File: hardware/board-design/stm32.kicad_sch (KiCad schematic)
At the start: 10 parts, among them J2 Conn_02x05_Odd_Even, SW1 SW_Push, U3 STM32C031C6Ux

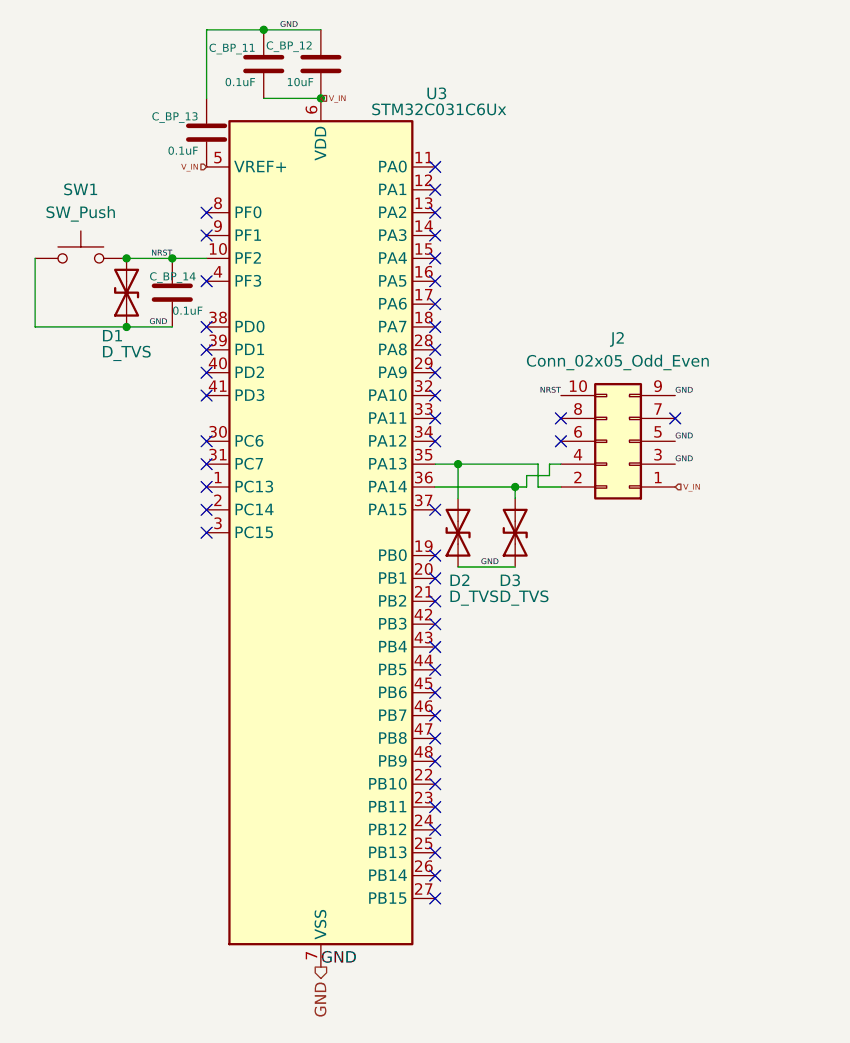
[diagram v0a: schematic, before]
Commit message: feat(stm32-schematic): add bmp180 and ssd1306
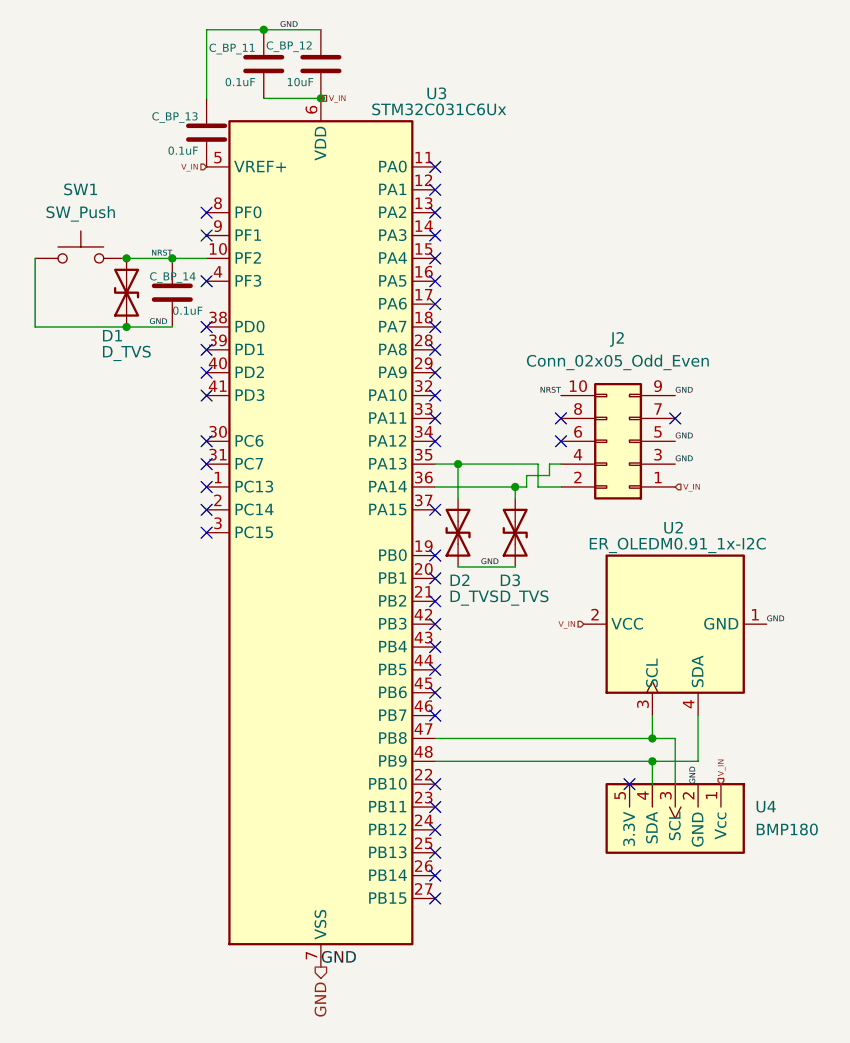
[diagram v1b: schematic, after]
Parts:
- added U2: ER_OLEDM0.91_1x-I2C, Display:ER_OLEDM0.91_1x-I2C, symbol Display_Graphic:ER_OLEDM0.91_1x-I2C
- added U4: BMP180, symbol MCU_Module:BMP180 GY-68
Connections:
- net GND: now also U2.1 (GND), U4.2 (GND)
- net V_IN: now also U2.2 (VCC), U4.1 (Vcc)
- net at U3.47 (PB8): now also U2.3 (SCL), U4.3 (SCL)
- net at U3.48 (PB9): now also U2.4 (SDA), U4.4 (SDA)
- no-connect marks 45 -> 44

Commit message: feat(component-properties): complate properties
Add datasheets, footprints, part numbers and manufacterer names
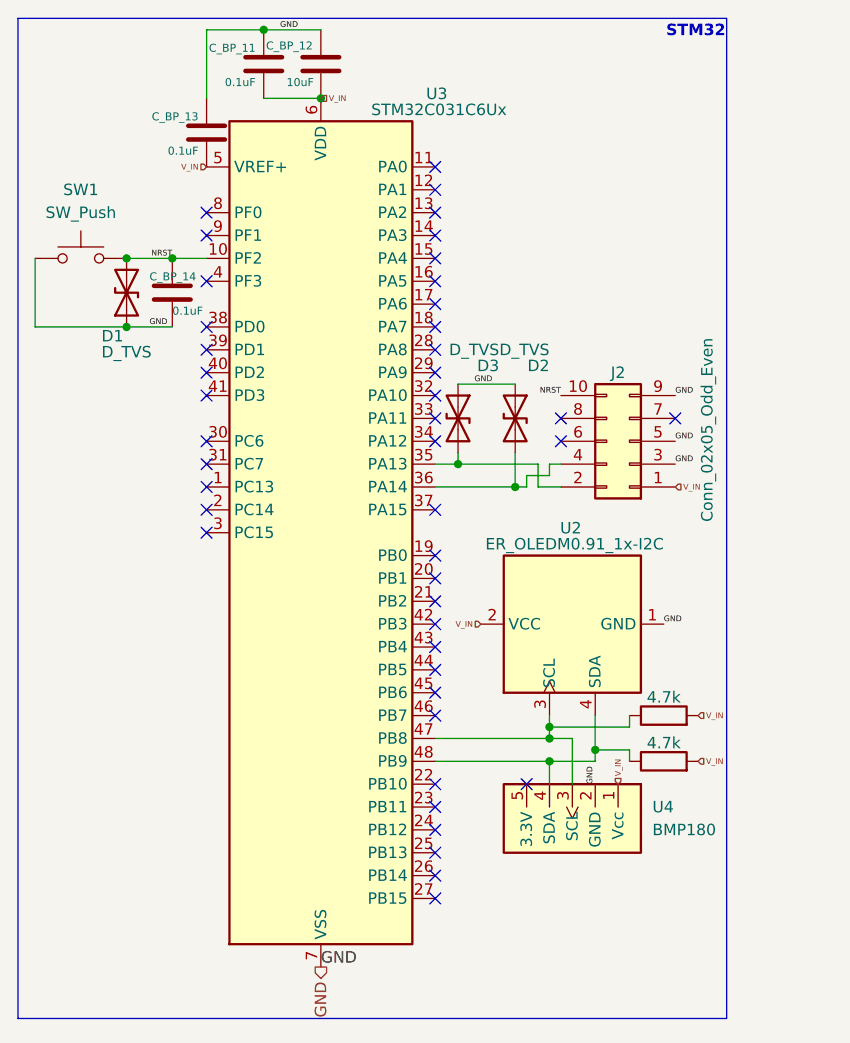
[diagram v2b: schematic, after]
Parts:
- added R1, R2: 4.7k, Resistor_SMD:R_0603_1608Metric_Pad0.98x0.95mm_HandSolder, symbol Device:R
- C_BP_11, C_BP_12, C_BP_13, C_BP_14: Manufacturer Murata -> Murata Electronics
- D1, D2, D3: footprint (none) -> Diode_SMD:D_SMA; Manufacturer (none) -> Littelfuse Inc.; PART NUMBER (none) -> SMAJ51A
- J2: footprint (none) -> Custom-lib:SAMTEC_FTE-105-01-G-DV; Manufacturer (none) -> Samtec Inc.; PART NUMBER (none) -> FTE-105-01-G-DV
- SW1: footprint (none) -> Button_Switch_SMD:SW_SPST_B3U-1000P-B; Manufacturer (none) -> Aratas; PART NUMBER (none) -> B3U-1000P
- U2: Manufacturer (none) -> SOLOMON SYSTECH; PART NUMBER (none) -> SSD1306
- U3: Manufacturer (none) -> STM; PART NUMBER (none) -> STM32C031C6U6
- U4: footprint (none) -> Custom-lib:GY-68; Manufacturer (none) -> Bosch; PART NUMBER (none) -> GY-68 BMP180
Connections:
- net V_IN: now also R1.2, R2.2
- net at J2.2 (Pin_2), U3.35 (PA13): now also D3.2 (A2); no longer D2.2 (A2)
- net at J2.4 (Pin_4), U3.36 (PA14): now also D2.2 (A2); no longer D3.2 (A2)
- net at U2.3 (SCL), U3.47 (PB8), U4.3 (SCL): now also R1.1
- net at U2.4 (SDA), U3.48 (PB9), U4.4 (SDA): now also R2.1
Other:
- note added: "STM32"
- moved on the sheet: U2, U4

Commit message: feat(sch): complate project rev 1.0
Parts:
- added C_STM_5, C_STM_7: 10uF, Custom-lib:CAPC6153X390N, symbol Device:C
- added C_STM_6, C_STM_8: 0.1uF, Capacitor_SMD:C_0603_1608Metric_Pad1.08x0.95mm_HandSolder, symbol Device:C
- C_STM_1: renamed from C_BP_13; Manufacturer Murata Electronics -> (none)
- C_STM_2: renamed from C_BP_14; Manufacturer Murata Electronics -> (none)
- C_STM_3: renamed from C_BP_11; Manufacturer Murata Electronics -> (none)
- C_STM_4: renamed from C_BP_12; Manufacturer Murata Electronics -> (none)
- D1, D2, D3: Manufacturer Littelfuse Inc. -> (none)
- J2: Manufacturer Samtec Inc. -> (none)
- R_OpenDrain1: renamed from R2; Manufacturer Vishay -> (none)
- R_OpenDrain2: renamed from R1; Manufacturer Vishay -> (none)
- SW1: Manufacturer Aratas -> (none)
- U2: Manufacturer SOLOMON SYSTECH -> (none)
- U3: Manufacturer STM -> (none)
- U4: Manufacturer Bosch -> (none); now in the parts list
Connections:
- net GND: now also J2.03 (Pin_3), J2.05 (Pin_5), J2.09 (Pin_9), C_STM_5.2, C_STM_6.2, C_STM_7.2, C_STM_8.1; no longer J2.3 (Pin_3), J2.5 (Pin_5), J2.9 (Pin_9)
- net V_IN: now also J2.01 (Pin_1), C_STM_5.1, C_STM_6.1, C_STM_7.1, C_STM_8.2; no longer J2.1 (Pin_1)
- net at D2.2 (A2), U3.36 (PA14): now also J2.04 (Pin_4); no longer J2.4 (Pin_4)
- net at D3.2 (A2), U3.35 (PA13): now also J2.02 (Pin_2); no longer J2.2 (Pin_2)
